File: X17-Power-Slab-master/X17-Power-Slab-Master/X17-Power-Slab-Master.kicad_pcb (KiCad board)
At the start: 2 copper layers, 129.5 x 119 mm, 4 parts

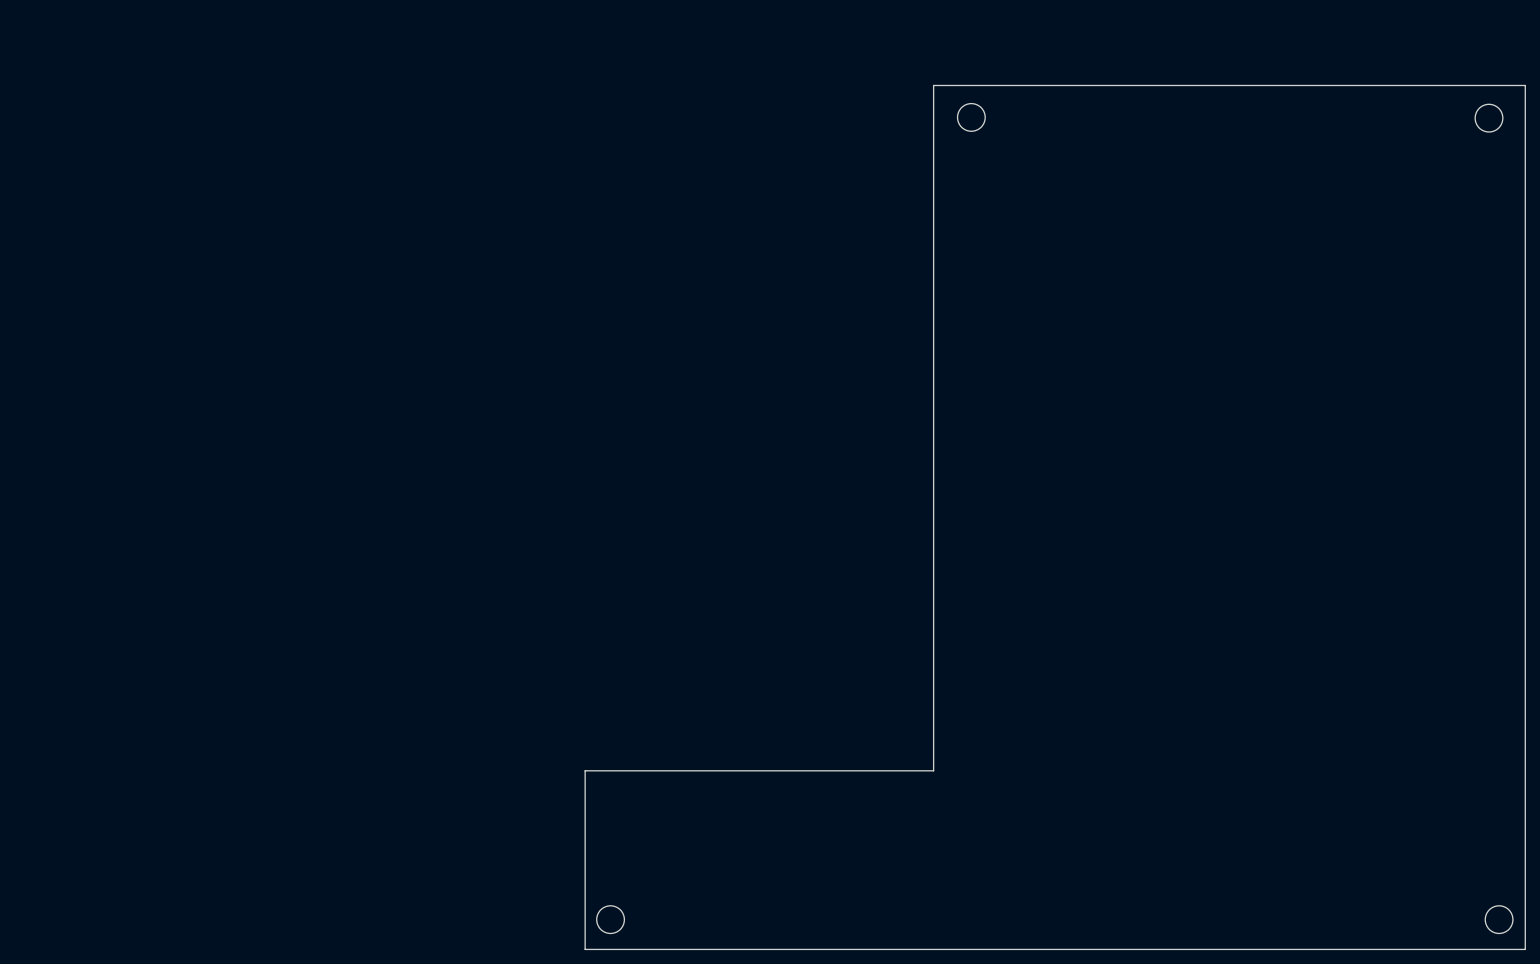
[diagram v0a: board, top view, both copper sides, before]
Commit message: Initial Placements
Issue - NRST_PSB is apparently ground flag
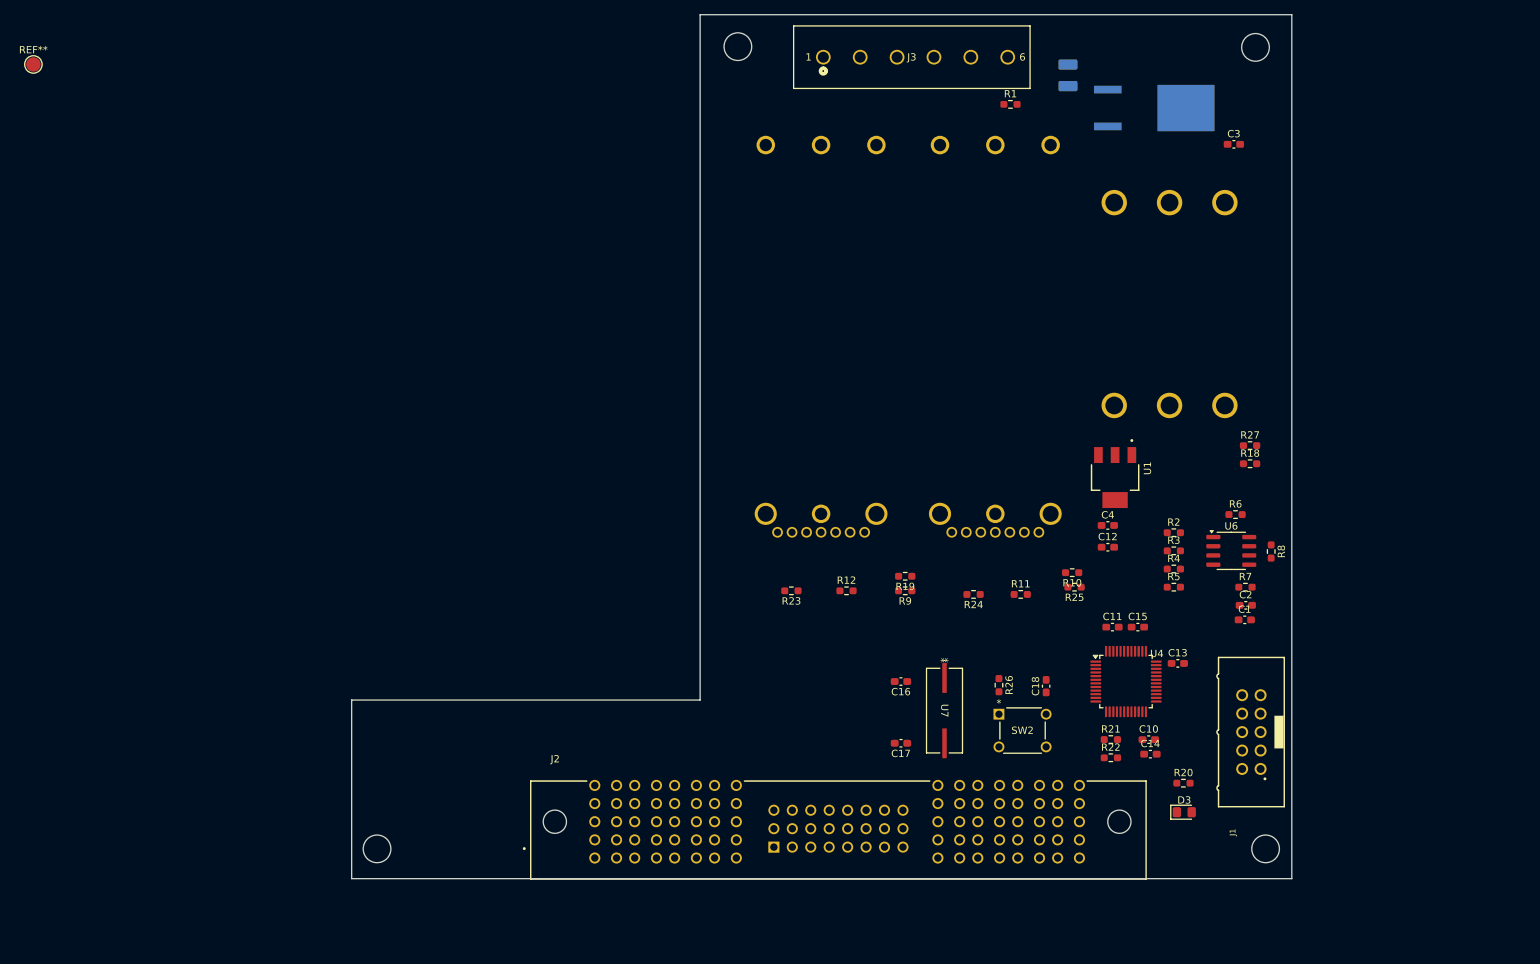
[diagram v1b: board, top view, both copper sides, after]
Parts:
- added C1: 10uF, Capacitor_SMD:C_0603_1608Metric_Pad1.08x0.95mm_HandSolder, F.Cu at (157.4, 106.0)
- added C10: 0.1uF, Capacitor_SMD:C_0603_1608Metric_Pad1.08x0.95mm_HandSolder, F.Cu at (144.1, 122.5)
- added C11: 0.1uF, Capacitor_SMD:C_0603_1608Metric_Pad1.08x0.95mm_HandSolder, F.Cu at (139.1, 107.0)
- added C12: 0.1uF, Capacitor_SMD:C_0603_1608Metric_Pad1.08x0.95mm_HandSolder, F.Cu at (138.5, 96.0)
- added C13: 0.1uF, Capacitor_SMD:C_0603_1608Metric_Pad1.08x0.95mm_HandSolder, F.Cu at (148.1, 112.0)
- added C14: 4.7uF, Capacitor_SMD:C_0603_1608Metric_Pad1.08x0.95mm_HandSolder, F.Cu at (144.4, 124.5)
- added C15: 4.7uF, Capacitor_SMD:C_0603_1608Metric_Pad1.08x0.95mm_HandSolder, F.Cu at (142.6, 107.0)
- added C16: 18pF, Capacitor_SMD:C_0603_1608Metric_Pad1.08x0.95mm_HandSolder, F.Cu at (110.0, 114.5)
- added C17: 18pF, Capacitor_SMD:C_0603_1608Metric_Pad1.08x0.95mm_HandSolder, F.Cu at (110.0, 123.0)
- added C18: 0.1uF, Capacitor_SMD:C_0603_1608Metric_Pad1.08x0.95mm_HandSolder, F.Cu at (130.0, 115.1)
- added C2: .1uF, Capacitor_SMD:C_0603_1608Metric_Pad1.08x0.95mm_HandSolder, F.Cu at (157.5, 104.0)
- added C3: 10uF, Capacitor_SMD:C_0603_1608Metric_Pad1.08x0.95mm_HandSolder, F.Cu at (155.9, 40.5)
- added C4: 22uF, Capacitor_SMD:C_0603_1608Metric_Pad1.08x0.95mm_HandSolder, F.Cu at (138.5, 93.0)
- added D1: SMB8J5.0CA-E3/52, Diode_SMD:D_1210_3225Metric_Pad1.42x2.65mm_HandSolder, B.Cu at (133.0, 31.0)
- added D3: LED, LED_SMD:LED_0805_2012Metric_Pad1.15x1.40mm_HandSolder, F.Cu at (149.0, 132.5)
- added J1: 61201021621, 612_STMconn:61201021621, F.Cu at (158.3, 121.5)
- added J2: ET60T-D04-3-08-D04-X-R1-S, ET60T-D04-3-08-D04-X-R1-S:SAMTEC_ET60T-D04-3-08-D04-X-R1-S, F.Cu at (101.2, 133.8)
- added J3: 796636-6, footprints:CON6_P5MM_VER_TERM-BLK_TYC, F.Cu at (99.3, 28.5)
- added Q2: IRF1018ESTRLPBF, Reverse Voltage Protection:TO254P1524X483-4, B.Cu at (144.9, 35.5)
- added R1: 10k, Resistor_SMD:R_0603_1608Metric_Pad0.98x0.95mm_HandSolder, F.Cu at (125.1, 35.0)
- added R10: 10k, Resistor_SMD:R_0603_1608Metric_Pad0.98x0.95mm_HandSolder, F.Cu at (133.6, 99.5)
- added R11: 10k, Resistor_SMD:R_0603_1608Metric_Pad0.98x0.95mm_HandSolder, F.Cu at (126.5, 102.5)
- added R12: 10k, Resistor_SMD:R_0603_1608Metric_Pad0.98x0.95mm_HandSolder, F.Cu at (102.5, 102.0)
- added R18: 10k, Resistor_SMD:R_0603_1608Metric_Pad0.98x0.95mm_HandSolder, F.Cu at (158.1, 84.5)
- added R19: 10k, Resistor_SMD:R_0603_1608Metric_Pad0.98x0.95mm_HandSolder, F.Cu at (110.6, 100.0)
- added R2: 10000, Resistor_SMD:R_0603_1608Metric_Pad0.98x0.95mm_HandSolder, F.Cu at (147.6, 94.0)
- added R20: 470, Resistor_SMD:R_0603_1608Metric_Pad0.98x0.95mm_HandSolder, F.Cu at (148.9, 128.5)
- added R21: 4.7k, Resistor_SMD:R_0603_1608Metric_Pad0.98x0.95mm_HandSolder, F.Cu at (138.9, 122.5)
- added R22: 4.7k, Resistor_SMD:R_0603_1608Metric_Pad0.98x0.95mm_HandSolder, F.Cu at (138.9, 125.0)
- added R23: 10k, Resistor_SMD:R_0603_1608Metric_Pad0.98x0.95mm_HandSolder, F.Cu at (94.9, 102.0)
- added R24: 10k, Resistor_SMD:R_0603_1608Metric_Pad0.98x0.95mm_HandSolder, F.Cu at (120.0, 102.5)
- added R25: 10k, Resistor_SMD:R_0603_1608Metric_Pad0.98x0.95mm_HandSolder, F.Cu at (133.9, 101.5)
- added R26: 10k, Resistor_SMD:R_0603_1608Metric_Pad0.98x0.95mm_HandSolder, F.Cu at (123.5, 115.0)
- added R27: 10k, Resistor_SMD:R_0603_1608Metric_Pad0.98x0.95mm_HandSolder, F.Cu at (158.1, 82.0)
- added R3: 10000, Resistor_SMD:R_0603_1608Metric_Pad0.98x0.95mm_HandSolder, F.Cu at (147.6, 96.5)
- added R4: 10000, Resistor_SMD:R_0603_1608Metric_Pad0.98x0.95mm_HandSolder, F.Cu at (147.6, 99.0)
- added R5: 10000, Resistor_SMD:R_0603_1608Metric_Pad0.98x0.95mm_HandSolder, F.Cu at (147.6, 101.5)
- added R6: 20000, Resistor_SMD:R_0603_1608Metric_Pad0.98x0.95mm_HandSolder, F.Cu at (156.1, 91.5)
- added R7: 20000, Resistor_SMD:R_0603_1608Metric_Pad0.98x0.95mm_HandSolder, F.Cu at (157.4, 101.5)
- added R8: 120, Resistor_SMD:R_0603_1608Metric_Pad0.98x0.95mm_HandSolder, F.Cu at (161.0, 96.6)
- added R9: 10k, Resistor_SMD:R_0603_1608Metric_Pad0.98x0.95mm_HandSolder, F.Cu at (110.6, 102.0)
- added REF**: TestPoint_Pad_D2.0mm, TestPoint:TestPoint_Pad_D2.0mm, F.Cu at (-9.50, 29.5)
- added SW2: 1825910-6, STM switch:SW4_1825910-B_TEC, F.Cu at (130.0, 123.5)
- added U1: AZ1117IH-3.3TRG1, AZ1117_4pin:SOT230P700X185-4N, F.Cu at (139.5, 86.4)
- added U2: ~, E48SC12030NRFH_Footprint:E48SC12030NRFH_Footprint, B.Cu at (99.0, 66.0)
- added U3: ~, E48SC12030NRFH_Footprint:E48SC12030NRFH_Footprint, B.Cu at (123.0, 66.0)
- added U4: STM32F091CCTx, Package_QFP:LQFP-48_7x7mm_P0.5mm, F.Cu at (141.0, 114.5)
- added U5: ~, 48Vto5V:PKU5000e, B.Cu at (147.0, 62.5)
- added U6: MAX485E, Package_SO:SOIC-8_3.9x4.9mm_P1.27mm, F.Cu at (155.5, 96.5)
- added U7: ABLS-8.000MHZ-B2-T, footprints:ABLS-8.000MHZ-B2-T_ABR, F.Cu at (116.0, 118.5)
- moved H1 33.6 mm to (87.5, 27.0)
- moved H1 33.6 mm to (37.8, 137.5)
- moved H3 33.6 mm to (160.2, 137.5)
- moved H4 33.6 mm to (158.8, 27.1)
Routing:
- net Net-(U5-Trim): track 0.00 -> 0.89 mm

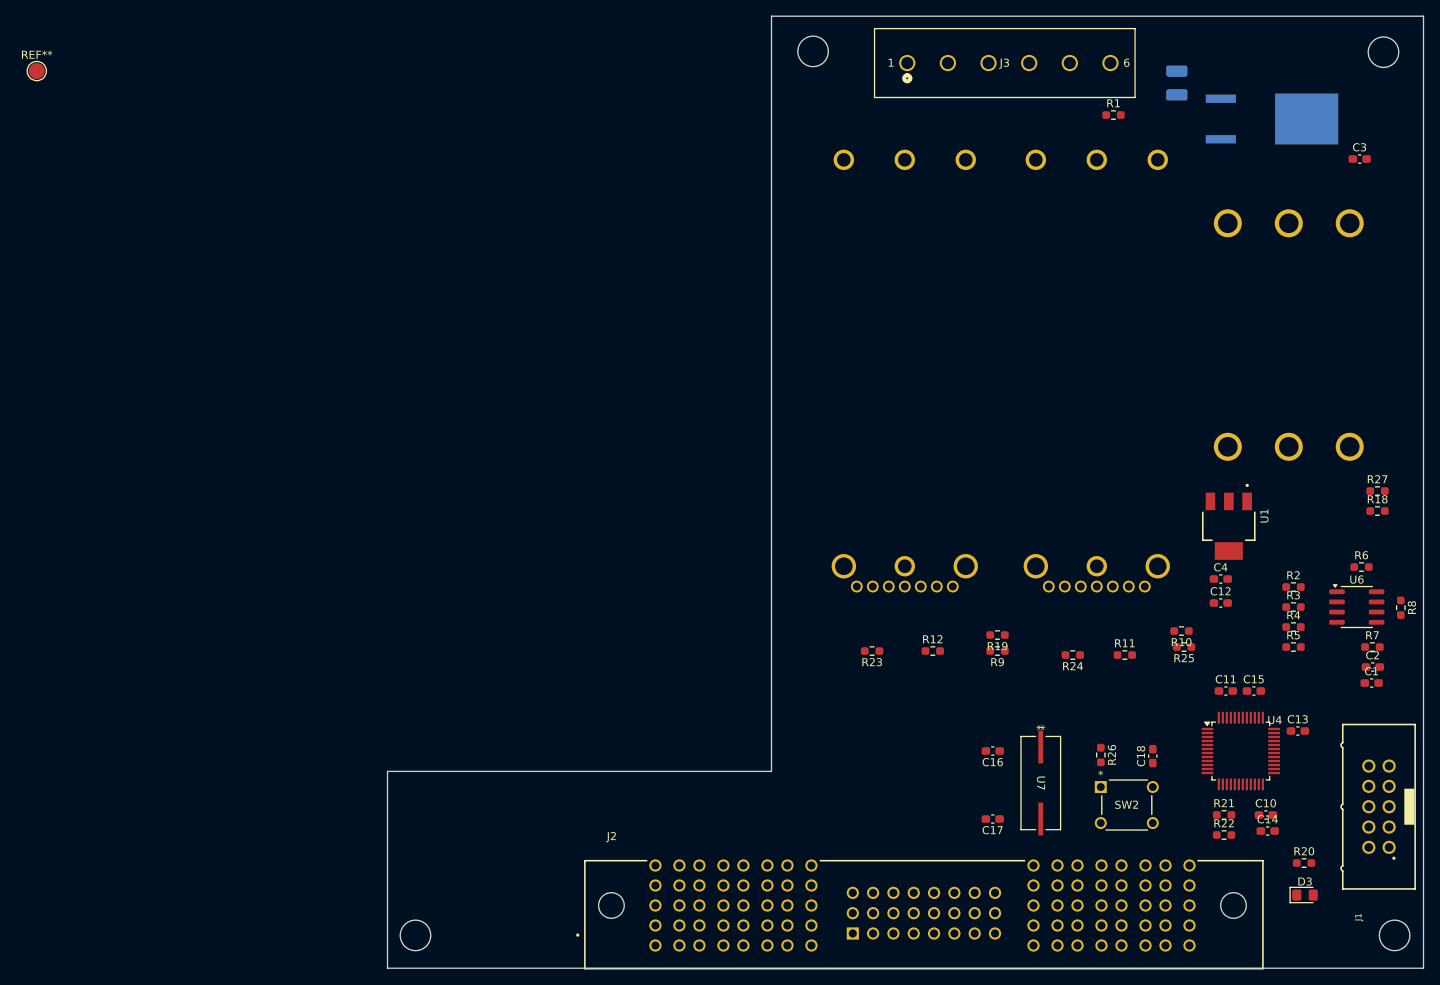
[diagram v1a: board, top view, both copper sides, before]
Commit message: Final First(?) Draft
NRST is stuck to general ground for whatever reason.

Test points wont connect for the life of me, will look @ in morning, will have sample plan.

Idea is there, really want to plan it out better 2nd time around. Alumni will give good tips!
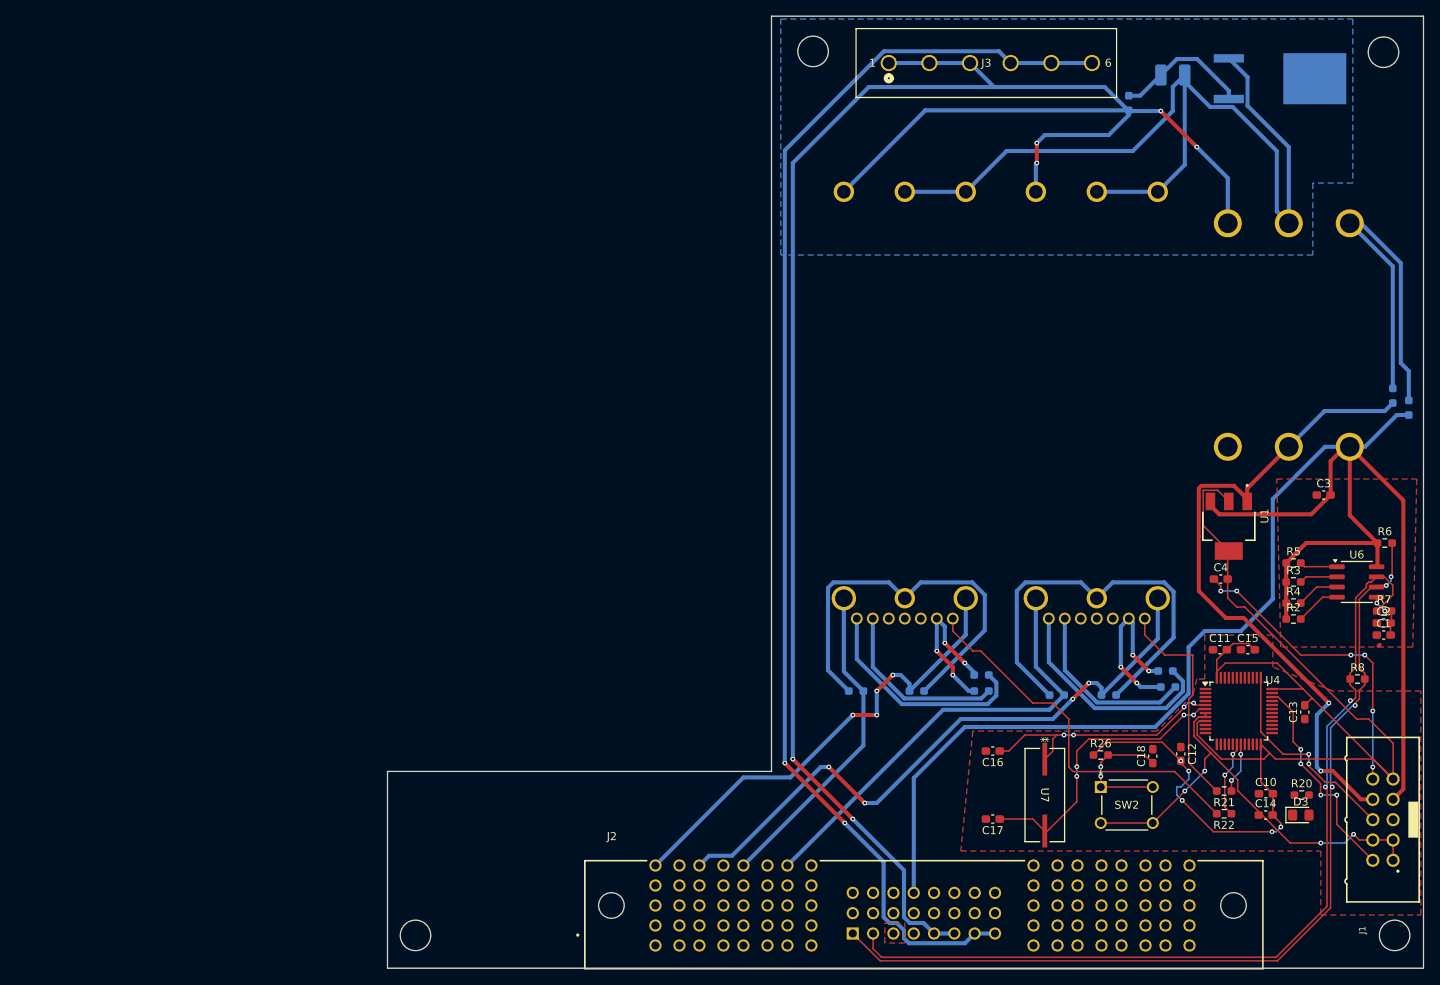
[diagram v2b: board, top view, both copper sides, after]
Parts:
- removed REF**: TestPoint_Pad_D2.0mm, TestPoint:TestPoint_Pad_D2.0mm
- R1, R10, R11, R12, R18, R19, R23, R24, R25, R27, R9: moved to B.Cu
- moved C3 42.2 mm to (151.4, 82.5)
- moved C12 19.5 mm to (133.5, 114.9), turned to -90 degrees
- moved R18 14.5 mm to (160.0, 70.1), turned to 90 degrees
- moved R27 11.1 mm to (162.0, 71.6), turned to 90 degrees
- moved R5 10.5 mm to (147.6, 91.0)
- moved R8 10.4 mm to (155.6, 105.5), turned to 0 degrees
- moved D3 10.0 mm to (148.5, 122.5)
- moved R20 8.51 mm to (148.6, 120.0)
- moved C1 6.18 mm to (158.9, 100.0)
- moved C2 5.67 mm to (158.9, 98.5)
- moved R10 5.39 mm to (131.6, 104.5), turned to 0 degrees
- moved R11 5.39 mm to (124.5, 107.5), turned to 180 degrees
- moved R12 5.39 mm to (100.5, 107.0), turned to 180 degrees
- moved R19 5.39 mm to (108.6, 105.0), turned to 0 degrees
- moved R23 5.39 mm to (92.9, 107.0), turned to 0 degrees
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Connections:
- C4 pad 1: NRST_PSB -> 3.3V_GND
- J1 pad 1: NRST -> NRST_PSB
- J1 pad 10: 5V_GND -> 3.3V_GND
- J1 pad 7: 3.3V -> 5V
- J1 pad 8: 3.3V_GND -> 5V_GND
- J1 pad 9: 5V -> 3.3V
- Q2 pad 4: GND_RAW -> NRST_PSB
- R27 pad 1: 5V_Out1 -> 5V
- U5 pad 4: 5V_Out1 -> 5V
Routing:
- net 48V_GND: track 0.00 -> 277.2 mm, vias 0 -> 2
- net 48V: track 0.00 -> 250.1 mm, vias 0 -> 6
- net 5V: track 0.00 -> 213.4 mm
- net 3.3V: track 0.00 -> 171.6 mm, vias 0 -> 5
- net 5V_GND: track 0.00 -> 125.2 mm, vias 0 -> 10
- net A+: track 0.00 -> 114.5 mm, vias 0 -> 4
- net A-: track 0.00 -> 113.1 mm, vias 0 -> 2
- net 12V_GND2: track 0.00 -> 79.6 mm, vias 0 -> 4
- net NRST_PSB: track 0.00 -> 62.9 mm, vias 0 -> 6
- net 12V_GND1: track 0.00 -> 59.3 mm, vias 0 -> 4
- net 12V_2: track 0.00 -> 57.0 mm
- net Net-(U3-TRIM): track 0.00 -> 52.8 mm
- net Net-(U2-TRIM): track 0.00 -> 51.3 mm
- net Net-(U5-Trim): track 0.89 -> 49.8 mm
- net C2_1: track 0.00 -> 47.5 mm
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- added copper zone on F.Cu, net 3.3V_GND
- added copper zone on B.Cu, net 48V_GND
- added copper zone on F.Cu, net 5V_GND
- added copper zone on F.Cu, net NRST_PSB
